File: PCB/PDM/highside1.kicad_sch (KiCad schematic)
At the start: 8 parts, among them Q10 STL225N6F7AG, Q11 STL225N6F7AG, Q4 STL135N8F7AG, Q5 STL135N8F7AG, Q6 STL135N8F7AG, Q7 STL135N8F7AG, Q8 STL135N8F7AG, Q9 STL135N8F7AG

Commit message: Changed MCP2561 to SN65HVD230 for Q1 and 3.3V supply
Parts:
- Q10, Q11: footprint POWERFLAT_5X6 -> PDM_Additional:POWERFLAT_5X6
- Q4, Q5, Q6, Q7, Q8, Q9: footprint STL135N8F7AG -> PDM_Additional:STL135N8F7AG
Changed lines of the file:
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@@
       (effects (font (size 1.27 1.27)) (justify right))
     )
-    (property "Footprint" "STL135N8F7AG" (id 2) (at 173.99 74.93 0)
+    (property "Footprint" "PDM_Additional:STL135N8F7AG" (id 2) (at 173.99 74.93 0)
       (effects (font (size 1.27 1.27)) (justify left) hide)
     )
@@
       (effects (font (size 1.27 1.27)) (justify right))
     )
-    (property "Footprint" "STL135N8F7AG" (id 2) (at 173.99 172.72 0)
+    (property "Footprint" "PDM_Additional:STL135N8F7AG" (id 2) (at 173.99 172.72 0)
       (effects (font (size 1.27 1.27)) (justify left) hide)
     )
@@
       (effects (font (size 1.27 1.27)) (justify left))
     )
-    (property "Footprint" "POWERFLAT_5X6" (id 2) (at 255.27 74.93 0)
+    (property "Footprint" "PDM_Additional:POWERFLAT_5X6" (id 2) (at 255.27 74.93 0)
       (effects (font (size 1.27 1.27)) (justify left) hide)
     )
@@
       (effects (font (size 1.27 1.27)) (justify right))
     )
-    (property "Footprint" "STL135N8F7AG" (id 2) (at 173.99 123.19 0)
+    (property "Footprint" "PDM_Additional:STL135N8F7AG" (id 2) (at 173.99 123.19 0)
       (effects (font (size 1.27 1.27)) (justify left) hide)
     )
@@
       (effects (font (size 1.27 1.27)) (justify right))
     )
-    (property "Footprint" "STL135N8F7AG" (id 2) (at 84.455 123.19 0)
+    (property "Footprint" "PDM_Additional:STL135N8F7AG" (id 2) (at 84.455 123.19 0)
       (effects (font (size 1.27 1.27)) (justify left) hide)
     )
@@
       (effects (font (size 1.27 1.27)) (justify right))
     )
-    (property "Footprint" "STL135N8F7AG" (id 2) (at 84.455 172.72 0)
+    (property "Footprint" "PDM_Additional:STL135N8F7AG" (id 2) (at 84.455 172.72 0)
       (effects (font (size 1.27 1.27)) (justify left) hide)
     )
@@
       (effects (font (size 1.27 1.27)) (justify right))
     )
-    (property "Footprint" "STL135N8F7AG" (id 2) (at 84.455 74.93 0)
+    (property "Footprint" "PDM_Additional:STL135N8F7AG" (id 2) (at 84.455 74.93 0)
       (effects (font (size 1.27 1.27)) (justify left) hide)
     )
@@
       (effects (font (size 1.27 1.27)) (justify left))
     )
-    (property "Footprint" "POWERFLAT_5X6" (id 2) (at 255.27 123.19 0)
-      (effects (font (size 1.27 1.27)) (justify left) hide)
-    )
+    (property "Footprint" "PDM_Additional:POWERFLAT_5X6" (id 2) (at 255.27 123.19 0)
+      (effects (font (size 1.27 1.27)) (justify left) hide)
+    )

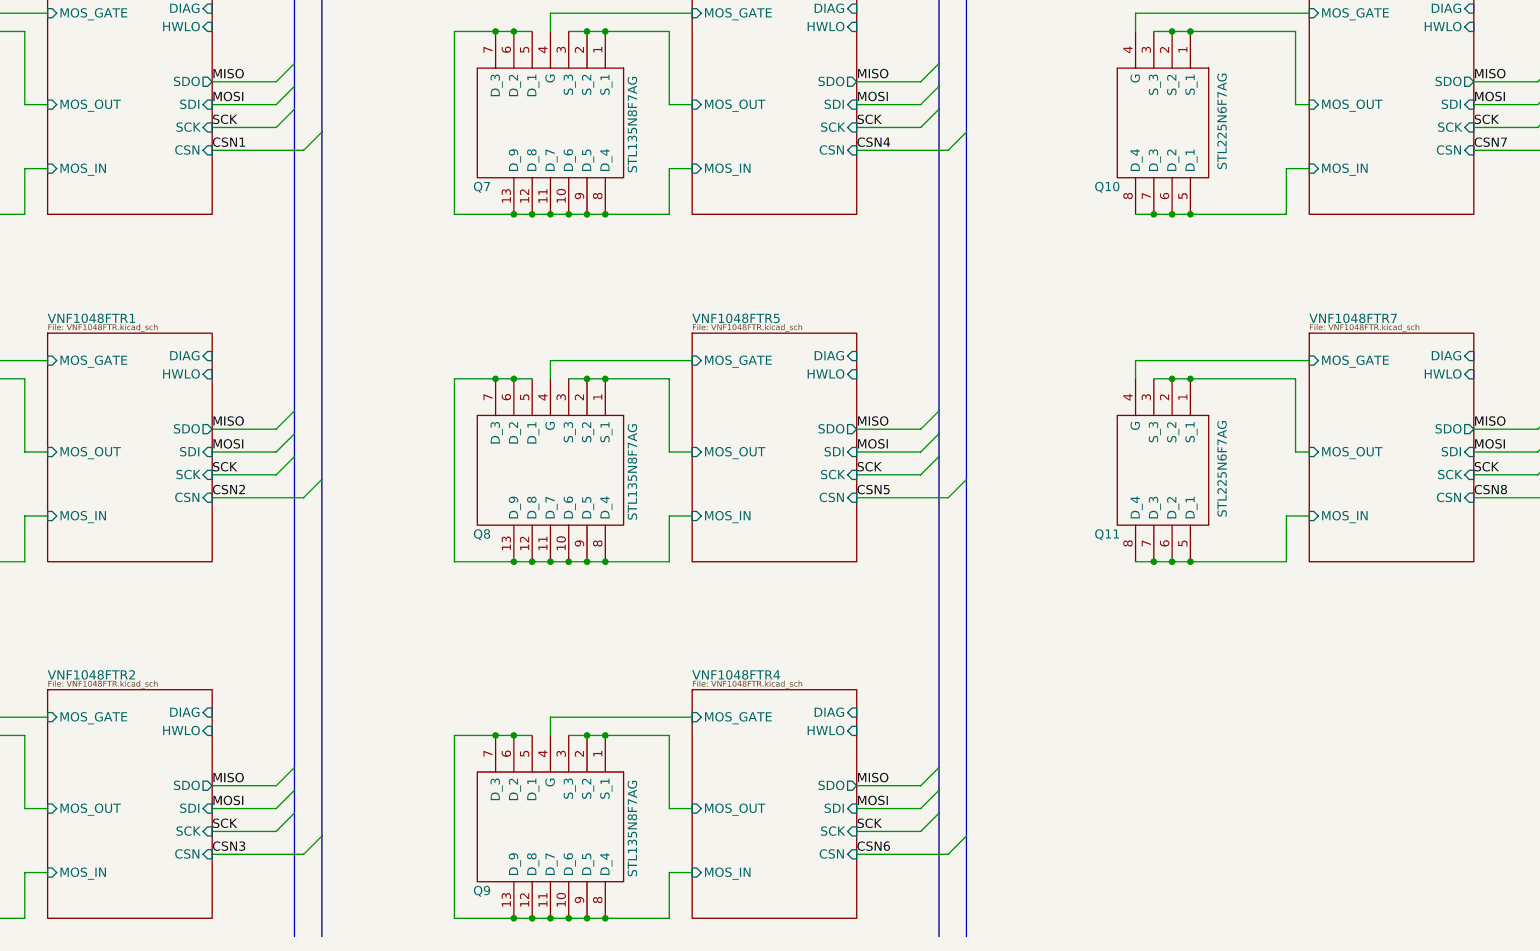
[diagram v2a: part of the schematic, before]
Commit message: Added fuse on each output of hs section - change footprint later!
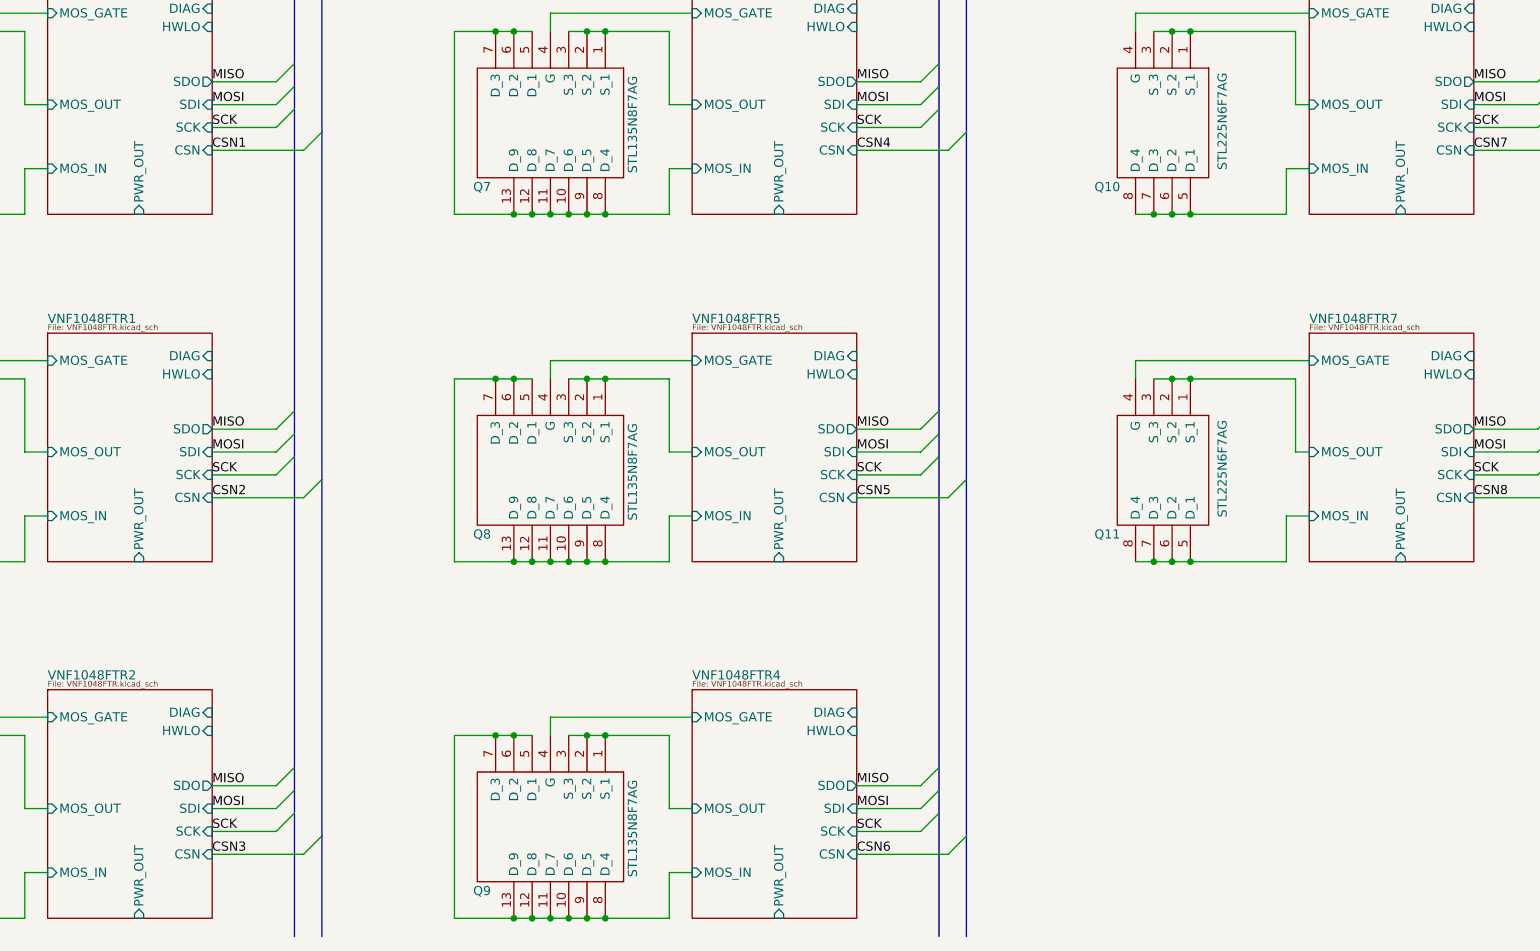
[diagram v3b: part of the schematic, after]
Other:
- sheet VNF1048FTR ports: added PWR_OUT; removed none
- sheet VNF1048FTR1 ports: added PWR_OUT; removed none
- sheet VNF1048FTR2 ports: added PWR_OUT; removed none
- sheet VNF1048FTR3 ports: added PWR_OUT; removed none
- sheet VNF1048FTR4 ports: added PWR_OUT; removed none
- sheet VNF1048FTR5 ports: added PWR_OUT; removed none
- sheet VNF1048FTR6 ports: added PWR_OUT; removed none
- sheet VNF1048FTR7 ports: added PWR_OUT; removed none
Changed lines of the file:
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@@
       (effects (font (size 1.27 1.27)) (justify right))
+    )
+    (pin "PWR_OUT" input (at 281.94 127 270)
+      (effects (font (size 1.27 1.27)) (justify left))
     )
   )
@@
       (effects (font (size 1.27 1.27)) (justify right))
     )
+    (pin "PWR_OUT" input (at 195.58 78.74 270)
+      (effects (font (size 1.27 1.27)) (justify left))
+    )
   )
   (sheet (at 93.98 144.78) (size 22.86 31.75)
@@
       (effects (font (size 1.27 1.27)) (justify right))
     )
+    (pin "PWR_OUT" input (at 106.68 176.53 270)
+      (effects (font (size 1.27 1.27)) (justify left))
+    )
   )
   (sheet (at 269.24 46.99) (size 22.86 31.75)
@@
       (effects (font (size 1.27 1.27)) (justify right))
     )
+    (pin "PWR_OUT" input (at 281.94 78.74 270)
+      (effects (font (size 1.27 1.27)) (justify left))
+    )
   )
   (sheet (at 183.515 95.25) (size 22.86 31.75)
@@
       (effects (font (size 1.27 1.27)) (justify right))
     )
+    (pin "PWR_OUT" input (at 195.58 127 270)
+      (effects (font (size 1.27 1.27)) (justify left))
+    )
   )
   (sheet (at 183.515 144.78) (size 22.86 31.75)
@@
       (effects (font (size 1.27 1.27)) (justify right))
     )
+    (pin "PWR_OUT" input (at 195.58 176.53 270)
+      (effects (font (size 1.27 1.27)) (justify left))
+    )
   )
   (sheet (at 93.98 95.25) (size 22.86 31.75)
@@
       (effects (font (size 1.27 1.27)) (justify right))
     )
+    (pin "PWR_OUT" input (at 106.68 127 270)
+      (effects (font (size 1.27 1.27)) (justify left))
+    )
   )
   (sheet (at 93.98 46.99) (size 22.86 31.75)
@@
       (effects (font (size 1.27 1.27)) (justify right))
     )
-  )
+    (pin "PWR_OUT" input (at 106.68 78.74 270)
+      (effects (font (size 1.27 1.27)) (justify left))
+    )
+  )

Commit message: Added adc protection and HC header radsock
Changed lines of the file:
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@@
-    (stroke (width 0) (type default) (color 0 0 0 0))
-  )
-  (wire (pts (xy 90.805 101.6) (xy 81.915 101.6))
     (stroke (width 0) (type default) (color 0 0 0 0))
   )
@@
     (stroke (width 0) (type default) (color 0 0 0 0))
   )
+  (wire (pts (xy 81.915 101.6) (xy 90.805 101.6))
+    (stroke (width 0) (type default) (color 0 0 0 0))
+  )
